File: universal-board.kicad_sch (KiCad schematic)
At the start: 36 parts, among them J1 USB_C_Receptacle, J2 CONN_I2C_GROVE, J3 CONN_WS2812, Q1 BSS138, SW1 SW_RESET, SW2 SW_ACK, U1 USBLC6-2SC6, U2 USBLC6-2SC6, U3 ESP32-S3-WROOM-1, U4 AMS1117-3.3, U5 CH224K, U6 74AHCT1G125, U7 TSOP384xx

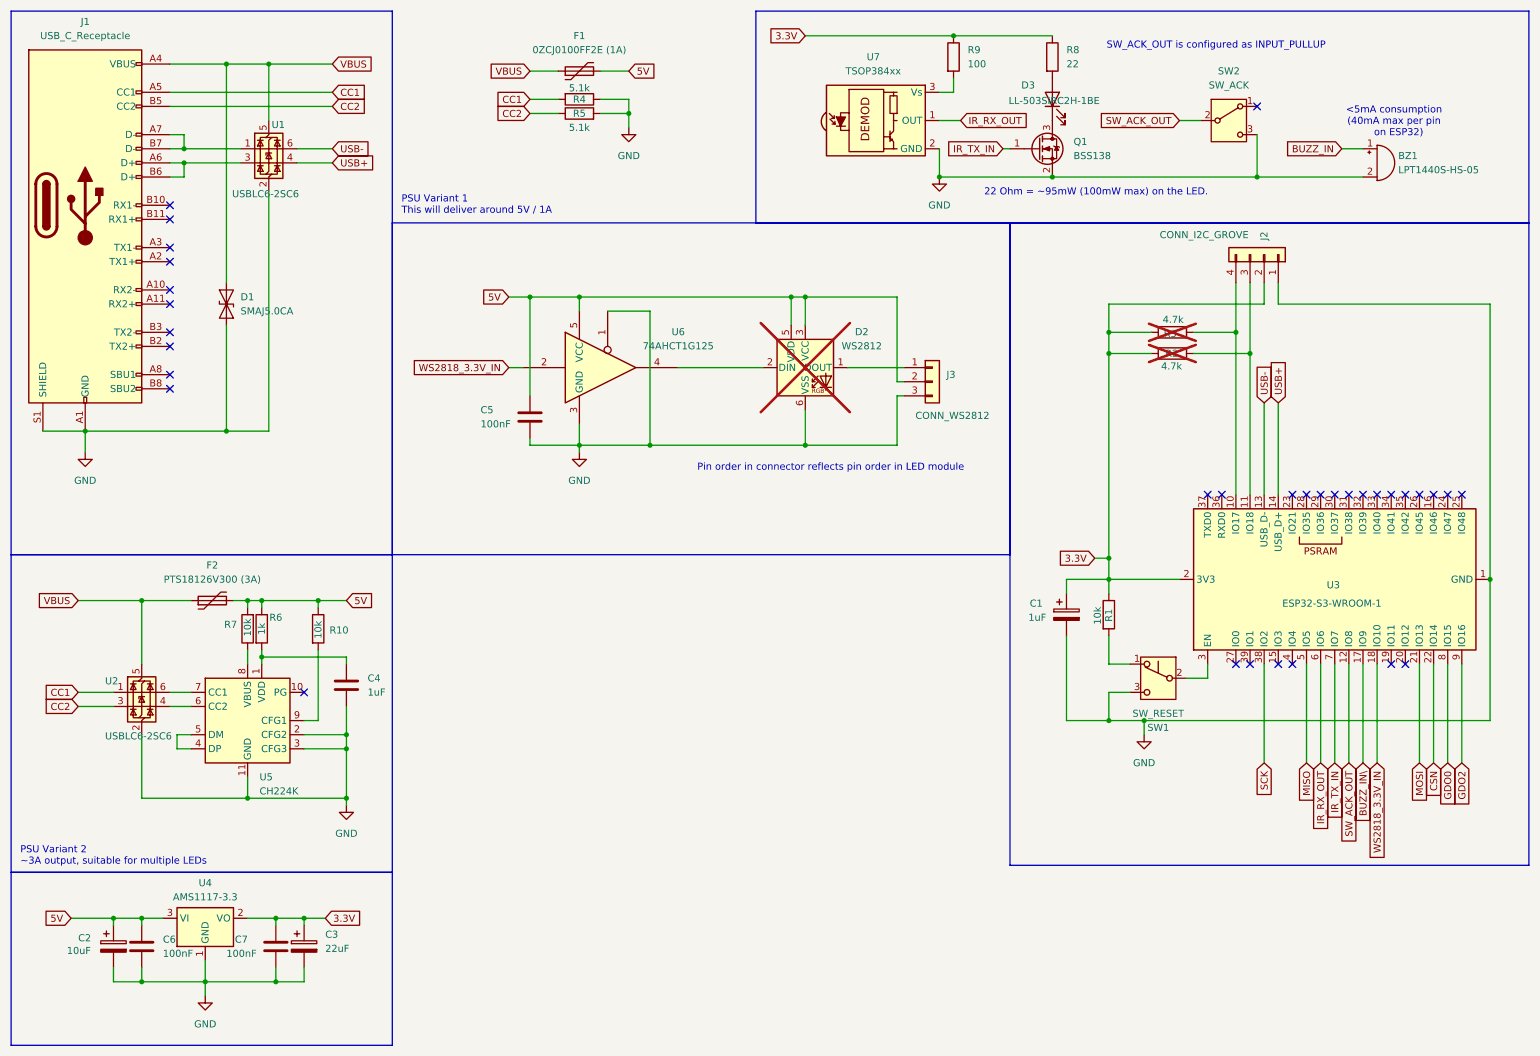
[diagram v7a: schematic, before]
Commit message: Remapped elements
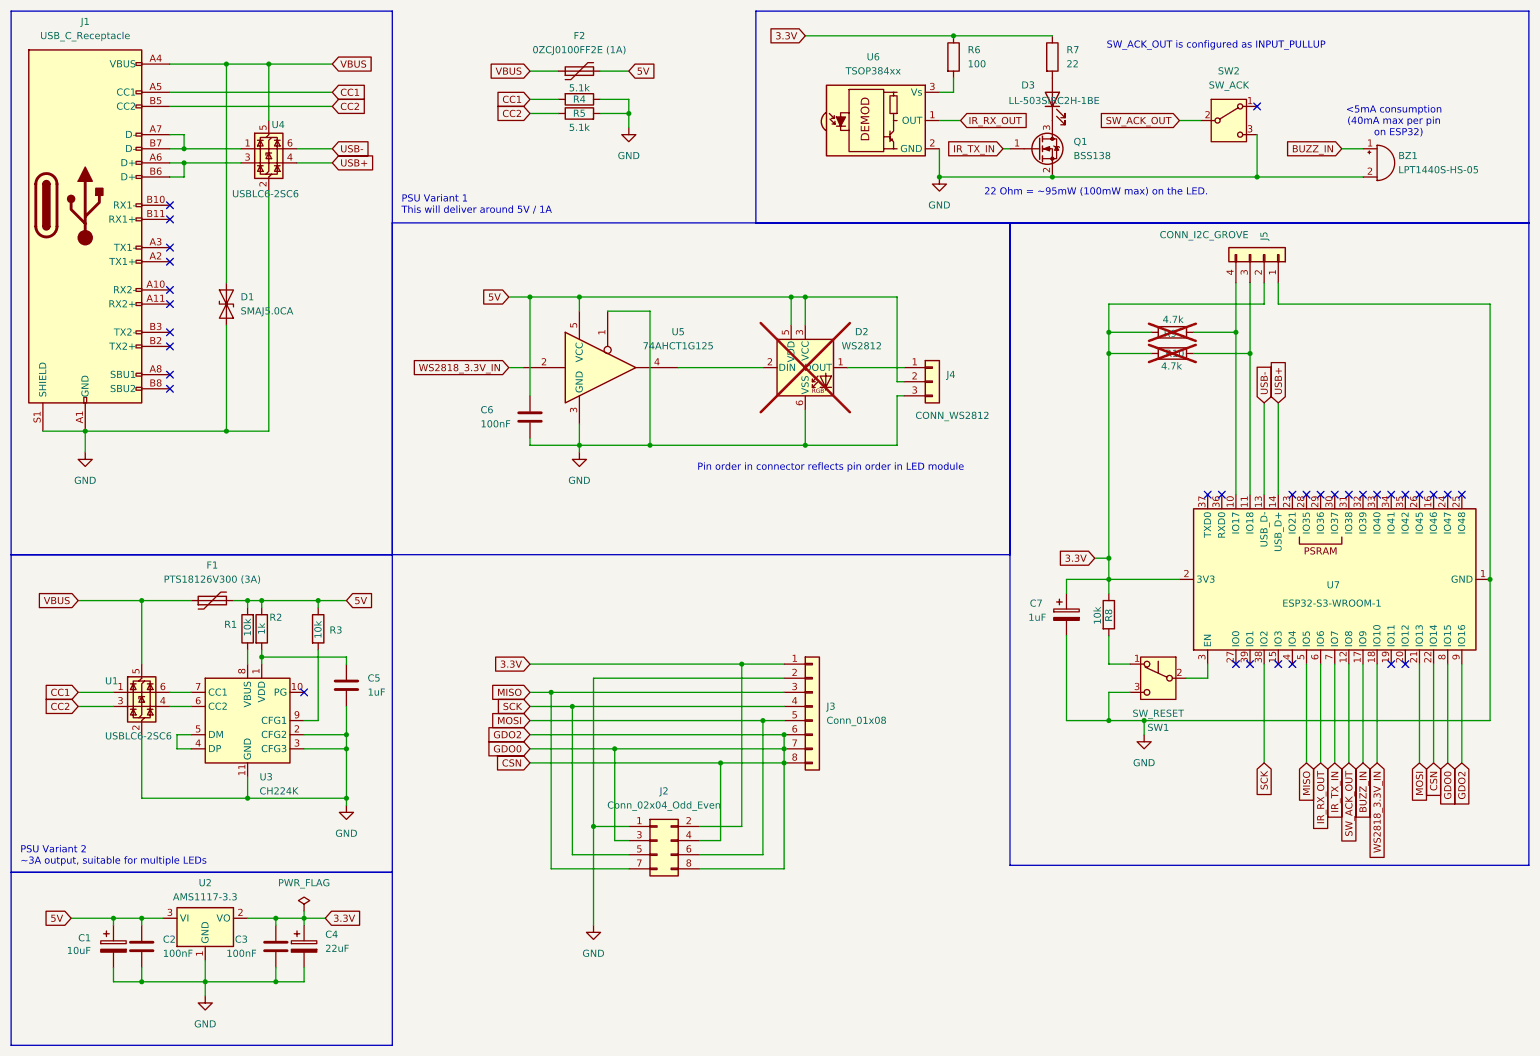
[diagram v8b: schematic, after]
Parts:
- added J2: Conn_02x04_Odd_Even, symbol Connector_Generic:Conn_02x04_Odd_Even
- added J3: Conn_01x08, symbol Connector_Generic:Conn_01x08
- renumbered C2 to C1, C6 to C2, C7 to C3, C3 to C4, C4 to C5, C5 to C6, C1 to C7, F2 to F1, F1 to F2, J3 to J4, J2 to J5, R7 to R1, R2 to R10, R6 to R2, R10 to R3, R9 to R6, R8 to R7, R1 to R8, R3 to R9, U2 to U1, U4 to U2, U5 to U3, U1 to U4, U6 to U5, U7 to U6, U3 to U7
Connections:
- net BUZZ_IN\ is gone; now on net BUZZ_IN: U7.17 (IO9)
- net GDO0 is gone; now on net CSN: U7.8 (IO15)
- net GDO2 is gone; now on net CSN: U7.9 (IO16)
- net 3.3V: now also J2.2 (Pin_2), J3.1 (Pin_1)
- net CSN: now also J2.3 (Pin_3), J2.4 (Pin_4), J2.8 (Pin_8), J3.6 (Pin_6), J3.7 (Pin_7), J3.8 (Pin_8)
- net GND: now also J2.1 (Pin_1), J3.2 (Pin_2)
- net MISO: now also J2.7 (Pin_7), J3.3 (Pin_3)
- net MOSI: now also J2.6 (Pin_6), J3.5 (Pin_5)
- net SCK: now also J2.5 (Pin_5), J3.4 (Pin_4)
